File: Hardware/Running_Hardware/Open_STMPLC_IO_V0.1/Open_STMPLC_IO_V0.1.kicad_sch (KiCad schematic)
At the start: 0 parts

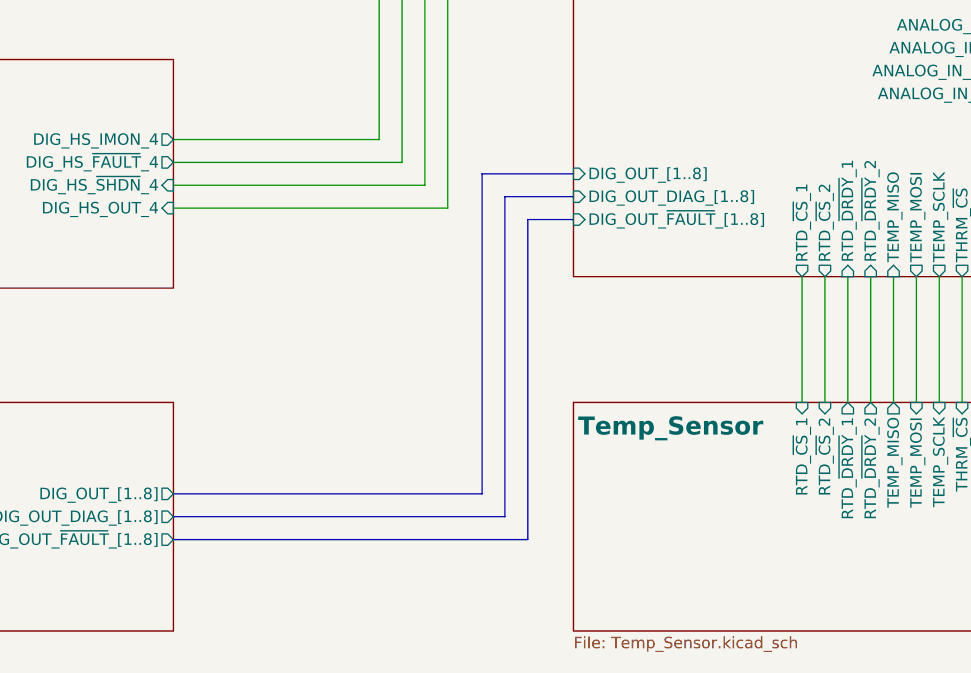
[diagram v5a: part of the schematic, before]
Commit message: Main PCB schematic changes V0.1
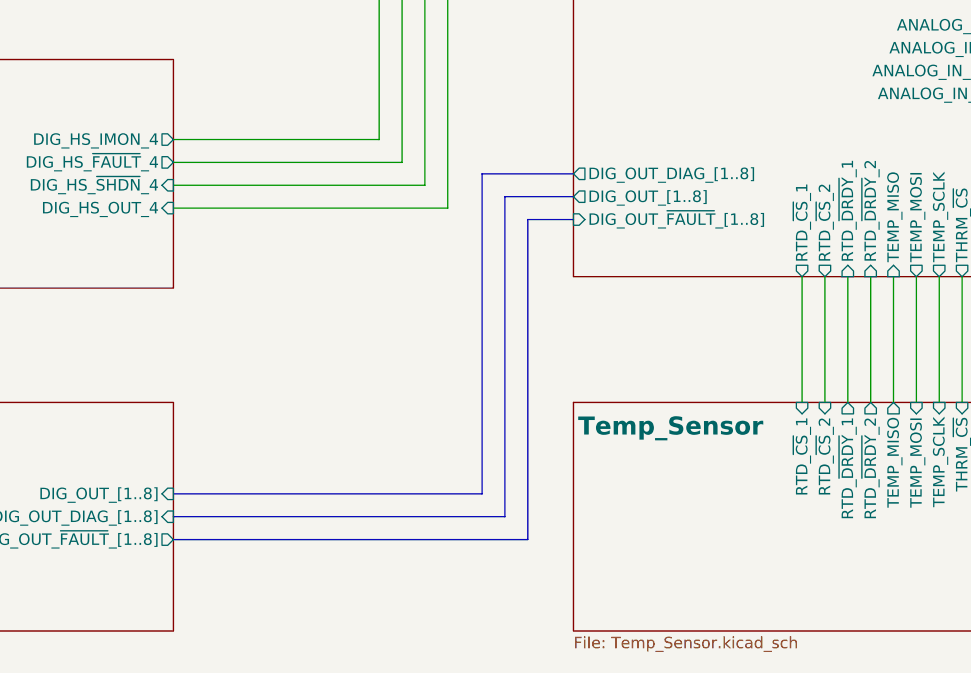
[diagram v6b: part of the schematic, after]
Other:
- title: Open_PLC_IO -> Open_STMPLC_IO
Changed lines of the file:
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@@
 	(paper "A4")
 	(title_block
-		(title "Open_PLC_IO")
-		(date "2026-04-01")
+		(title "Open_STMPLC_IO")
+		(date "2026-04-04")
 		(rev "0.1")
 	)
@@
 			)
 		)
-		(pin "DIG_OUT_DIAG_[1..8]" output
-			(at 68.58 175.26 0)
-			(effects
-				(font
-					(size 1.27 1.27)
-				)
-				(justify right)
-			)
-		)
-		(pin "DIG_OUT_[1..8]" output
-			(at 68.58 172.72 0)
-			(effects
-				(font
-					(size 1.27 1.27)
-				)
-				(justify right)
-			)
-		)
 		(pin "DIG_OUT_~{FAULT}_[1..8]" output
 			(at 68.58 177.8 0)
+			(effects
+				(font
+					(size 1.27 1.27)
+				)
+				(justify right)
+			)
+		)
+		(pin "DIG_OUT_DIAG_[1..8]" input
+			(at 68.58 175.26 0)
+			(effects
+				(font
+					(size 1.27 1.27)
+				)
+				(justify right)
+			)
+		)
+		(pin "DIG_OUT_[1..8]" input
+			(at 68.58 172.72 0)
 			(effects
 				(font
@@
 			)
 		)
-		(pin "DIG_OUT_DIAG_[1..8]" input
-			(at 113.03 139.7 180)
-			(effects
-				(font
-					(size 1.27 1.27)
-				)
-				(justify left)
-			)
-		)
-		(pin "DIG_OUT_[1..8]" input
-			(at 113.03 137.16 180)
-			(effects
-				(font
-					(size 1.27 1.27)
-				)
-				(justify left)
-			)
-		)
 		(pin "DIG_OUT_~{FAULT}_[1..8]" input
 			(at 113.03 142.24 180)
@@
 			)
 		)
+		(pin "DIG_OUT_DIAG_[1..8]" output
+			(at 113.03 137.16 180)
+			(effects
+				(font
+					(size 1.27 1.27)
+				)
+				(justify left)
+			)
+		)
+		(pin "DIG_OUT_[1..8]" output
+			(at 113.03 139.7 180)
+			(effects
+				(font
+					(size 1.27 1.27)
+				)
+				(justify left)
+			)
+		)

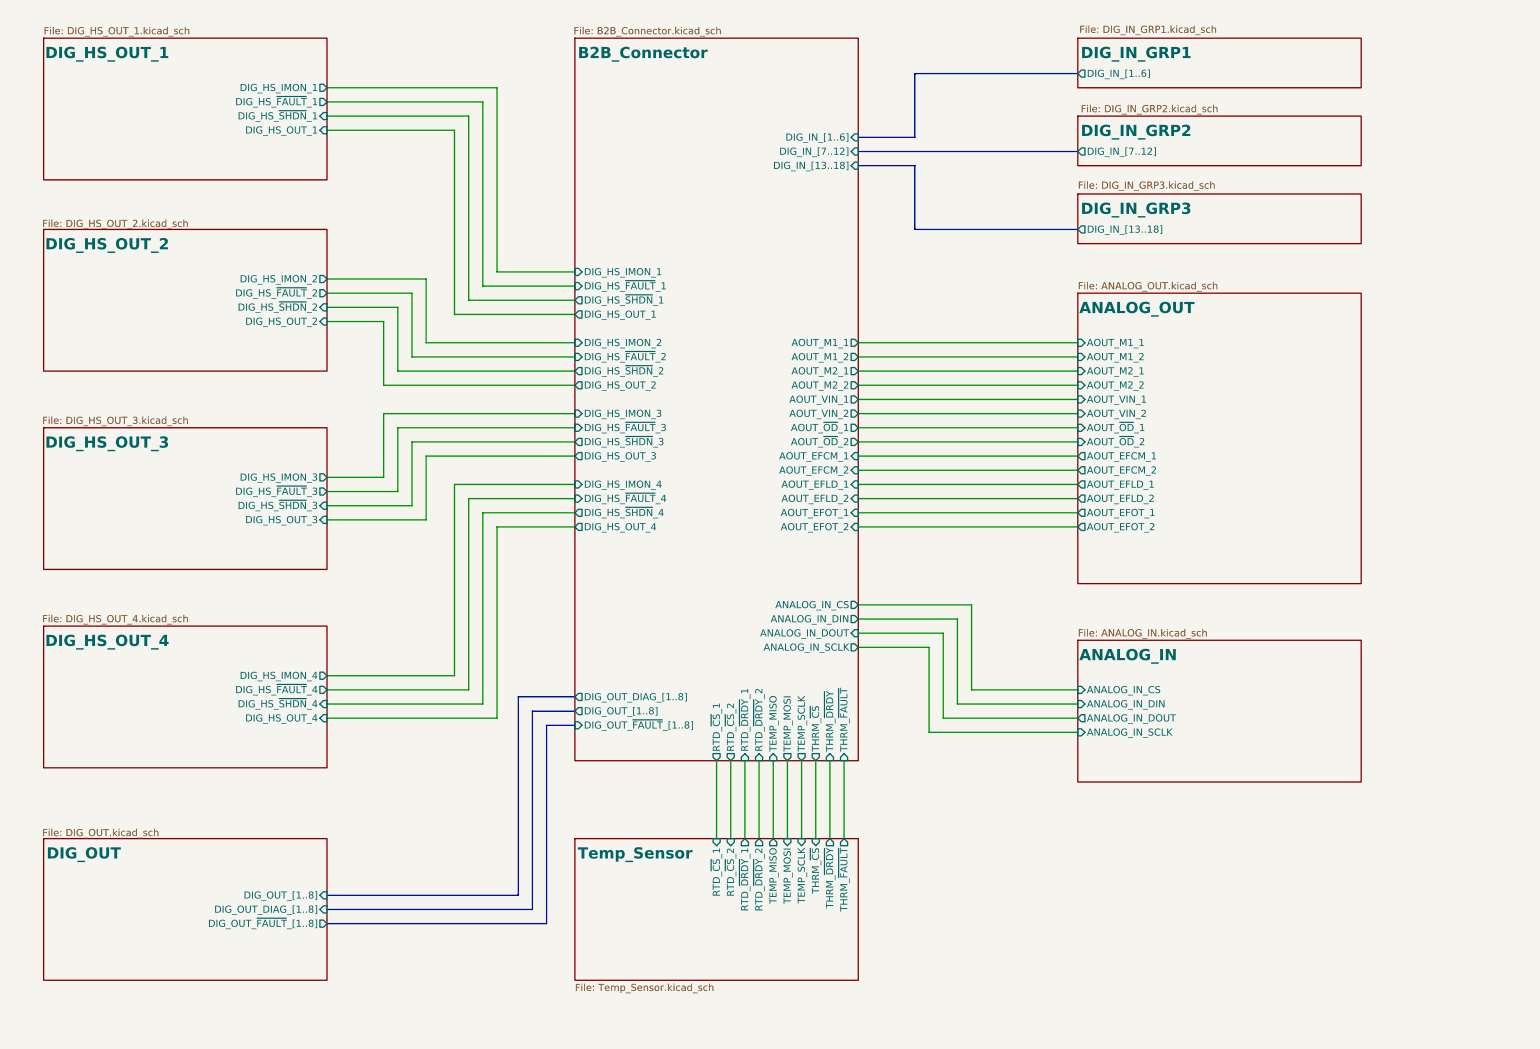
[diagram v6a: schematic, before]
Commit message: Common GND terminal changes
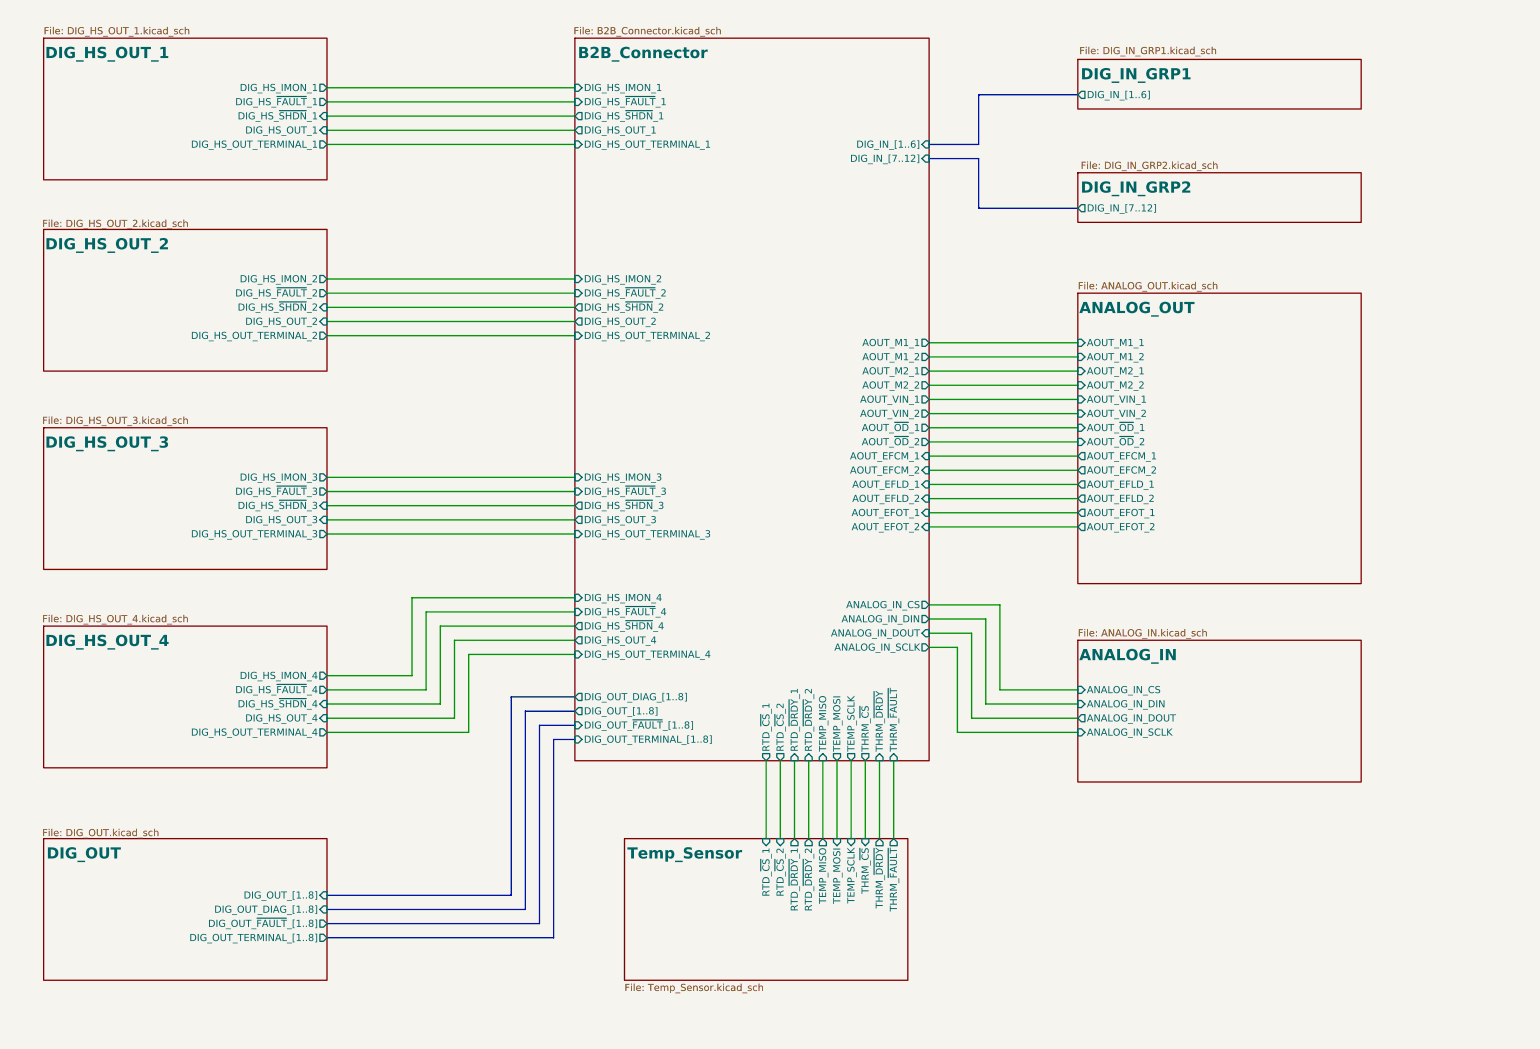
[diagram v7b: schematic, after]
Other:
- removed sheet DIG_IN_GRP3
- sheet B2B_Connector ports: added DIG_HS_OUT_TERMINAL_1, DIG_HS_OUT_TERMINAL_2, DIG_HS_OUT_TERMINAL_3, DIG_HS_OUT_TERMINAL_4, DIG_OUT_TERMINAL_[1..8]; removed DIG_IN_[13..18]
- sheet DIG_HS_OUT_1 ports: added DIG_HS_OUT_TERMINAL_1; removed none
- sheet DIG_HS_OUT_2 ports: added DIG_HS_OUT_TERMINAL_2; removed none
- sheet DIG_HS_OUT_3 ports: added DIG_HS_OUT_TERMINAL_3; removed none
- sheet DIG_HS_OUT_4 ports: added DIG_HS_OUT_TERMINAL_4; removed none
- sheet DIG_OUT ports: added DIG_OUT_TERMINAL_[1..8]; removed none

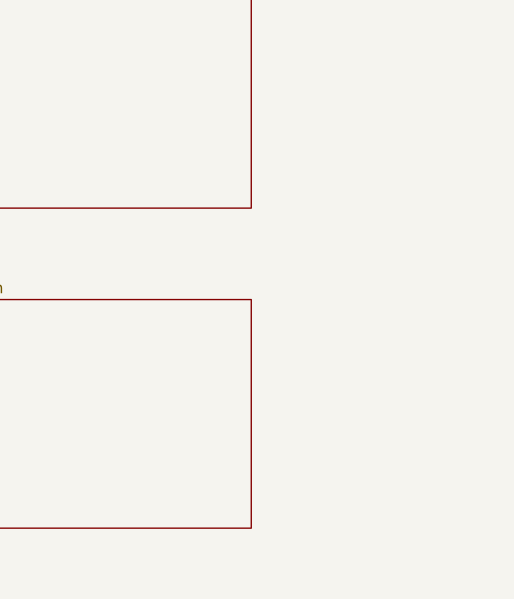
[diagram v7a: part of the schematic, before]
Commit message: IO board component placement
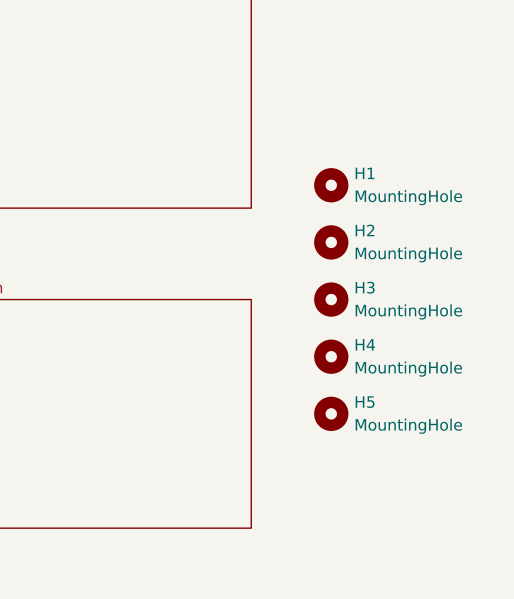
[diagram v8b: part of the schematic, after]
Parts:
- added H1, H2, H3, H4, H5: MountingHole, MountingHole:MountingHole_3.2mm_M3, symbol Mechanical:MountingHole
